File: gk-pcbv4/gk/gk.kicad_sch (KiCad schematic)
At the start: 11 parts

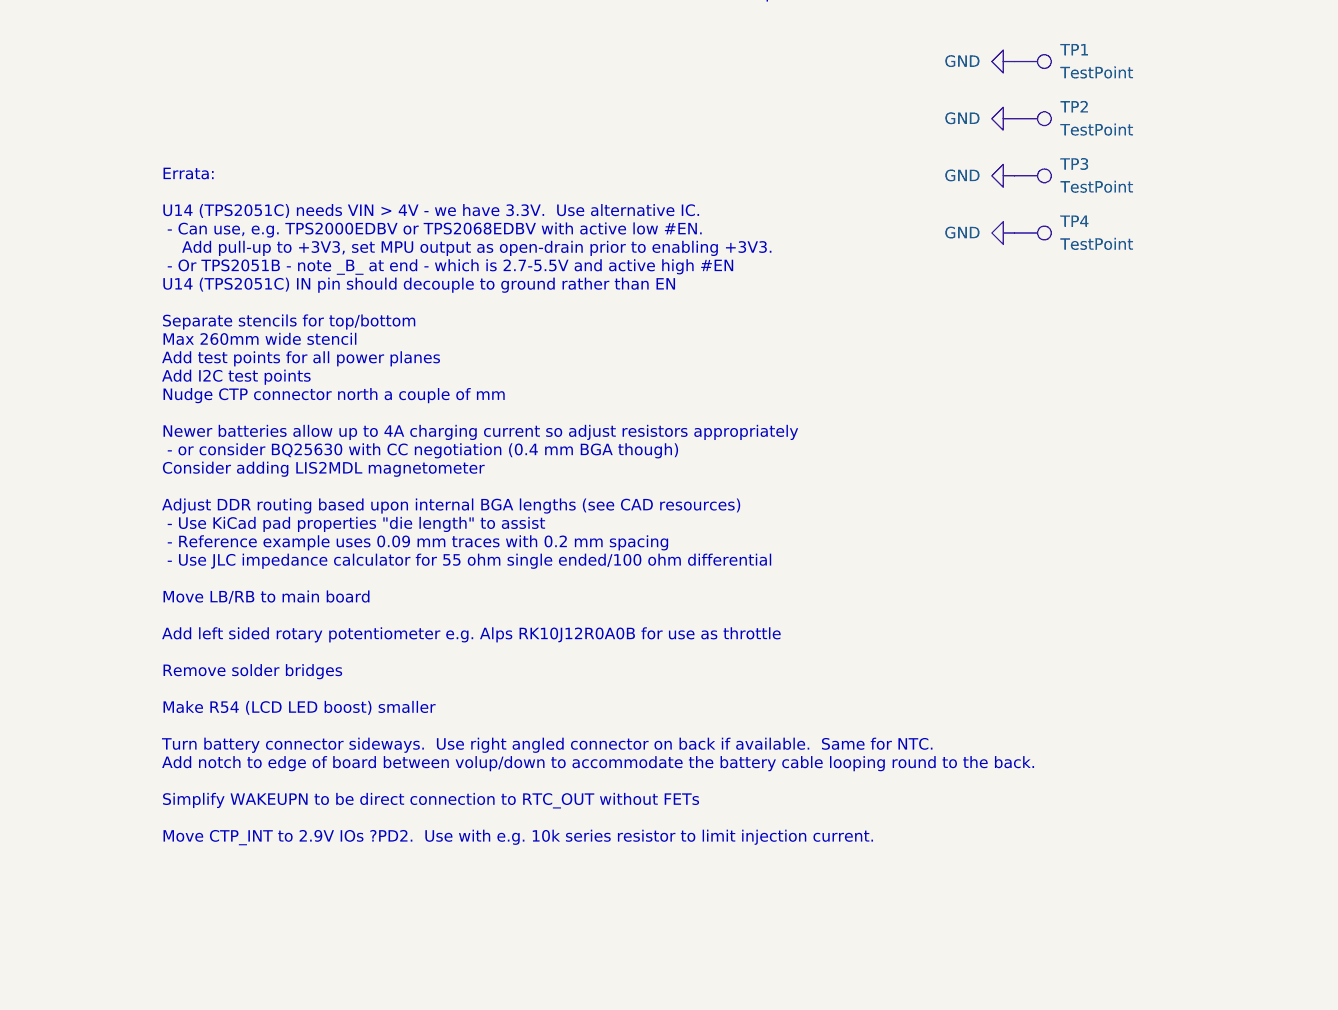
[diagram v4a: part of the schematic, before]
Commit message: Remove wakeupn mosfets in schematic
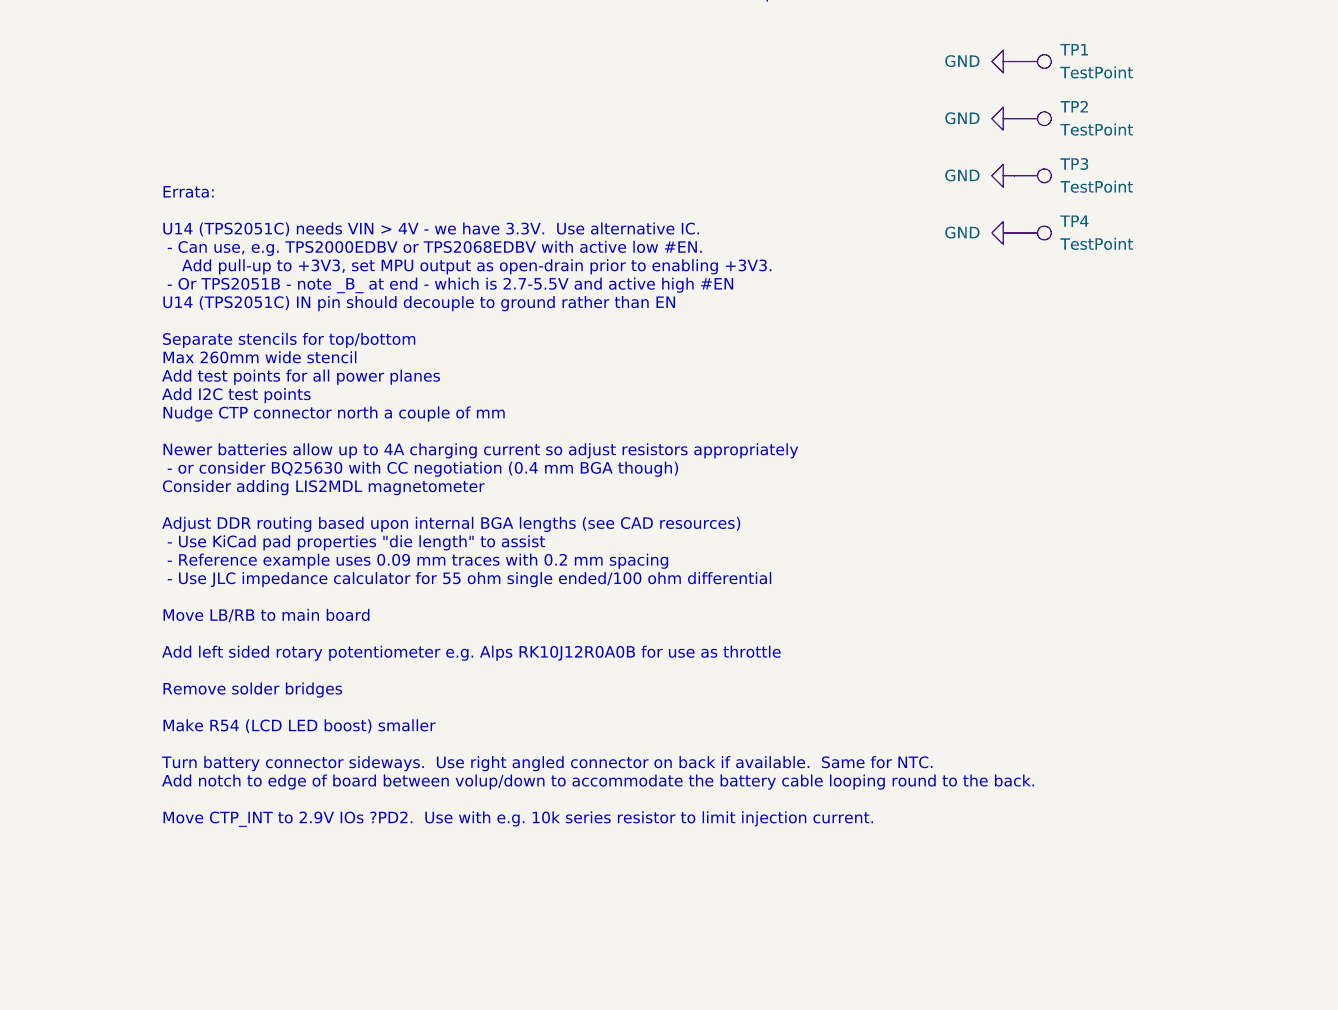
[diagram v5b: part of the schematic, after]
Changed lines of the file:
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@@
 		)
 	)
-	(text "Errata:\n\nU14 (TPS2051C) needs VIN > 4V - we have 3.3V.  Use alternative IC.\n - Can use, e.g. TPS2000EDBV or TPS2068EDBV with active low #EN.\n    Add pull-up to +3V3, set MPU output as open-drain prior to enabling +3V3.\n - Or TPS2051B - note _B_ at end - which is 2.7-5.5V and active high #EN\nU14 (TPS2051C) IN pin should decouple to ground rather than EN\n\nSeparate stencils for top/bottom\nMax 260mm wide stencil\nAdd test points for all power planes\nAdd I2C test points\nNudge CTP connector north a couple of mm\n\nNewer batteries allow up to 4A charging current so adjust resistors appropriately\n - or consider BQ25630 with CC negotiation (0.4 mm BGA though)\nConsider adding LIS2MDL magnetometer\n\nAdjust DDR routing based upon internal BGA lengths (see CAD resources)\n - Use KiCad pad properties \"die length\" to assist\n - Reference example uses 0.09 mm traces with 0.2 mm spacing\n - Use JLC impedance calculator for 55 ohm single ended/100 ohm differential\n\nMove LB/RB to main board\n\nAdd left sided rotary potentiometer e.g. Alps RK10J12R0A0B for use as throttle\n\nRemove solder bridges\n\nMake R54 (LCD LED boost) smaller\n\nTurn battery connector sideways.  Use right angled connector on back if available.  Same for NTC.\nAdd notch to edge of board between volup/down to accommodate the battery cable looping round to the back.\n\nSimplify WAKEUPN to be direct connection to RTC_OUT without FETs\n\nMove CTP_INT to 2.9V IOs ?PD2.  Use with e.g. 10k series resistor to limit injection current."
+	(text "Errata:\n\nU14 (TPS2051C) needs VIN > 4V - we have 3.3V.  Use alternative IC.\n - Can use, e.g. TPS2000EDBV or TPS2068EDBV with active low #EN.\n    Add pull-up to +3V3, set MPU output as open-drain prior to enabling +3V3.\n - Or TPS2051B - note _B_ at end - which is 2.7-5.5V and active high #EN\nU14 (TPS2051C) IN pin should decouple to ground rather than EN\n\nSeparate stencils for top/bottom\nMax 260mm wide stencil\nAdd test points for all power planes\nAdd I2C test points\nNudge CTP connector north a couple of mm\n\nNewer batteries allow up to 4A charging current so adjust resistors appropriately\n - or consider BQ25630 with CC negotiation (0.4 mm BGA though)\nConsider adding LIS2MDL magnetometer\n\nAdjust DDR routing based upon internal BGA lengths (see CAD resources)\n - Use KiCad pad properties \"die length\" to assist\n - Reference example uses 0.09 mm traces with 0.2 mm spacing\n - Use JLC impedance calculator for 55 ohm single ended/100 ohm differential\n\nMove LB/RB to main board\n\nAdd left sided rotary potentiometer e.g. Alps RK10J12R0A0B for use as throttle\n\nRemove solder bridges\n\nMake R54 (LCD LED boost) smaller\n\nTurn battery connector sideways.  Use right angled connector on back if available.  Same for NTC.\nAdd notch to edge of board between volup/down to accommodate the battery cable looping round to the back.\n\nMove CTP_INT to 2.9V IOs ?PD2.  Use with e.g. 10k series resistor to limit injection current."
 		(exclude_from_sim no)
 		(at 104.648 80.01 0)

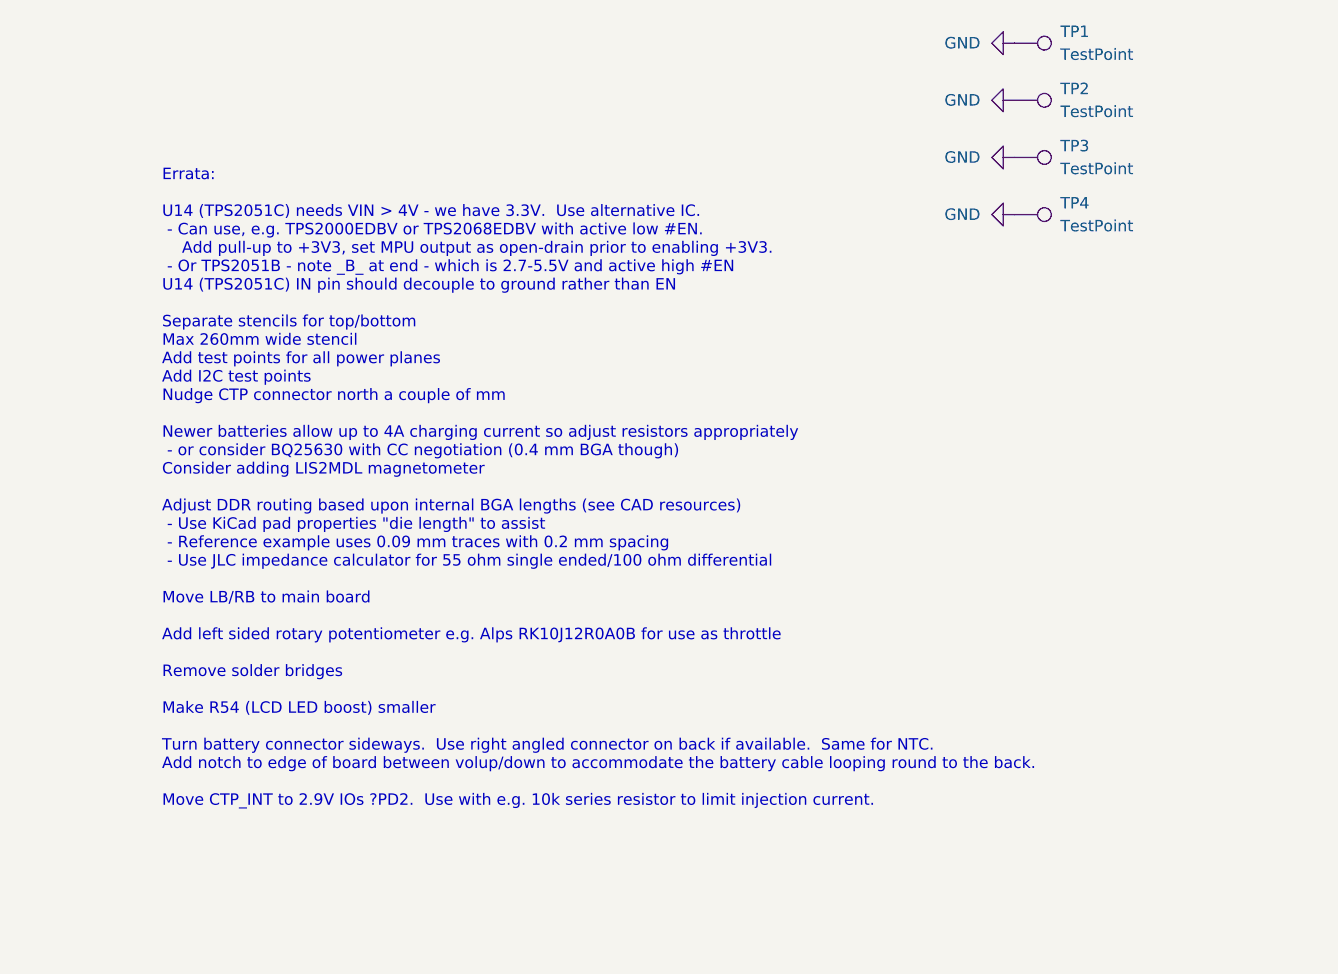
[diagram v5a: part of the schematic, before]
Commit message: update ctp irq resistor divider
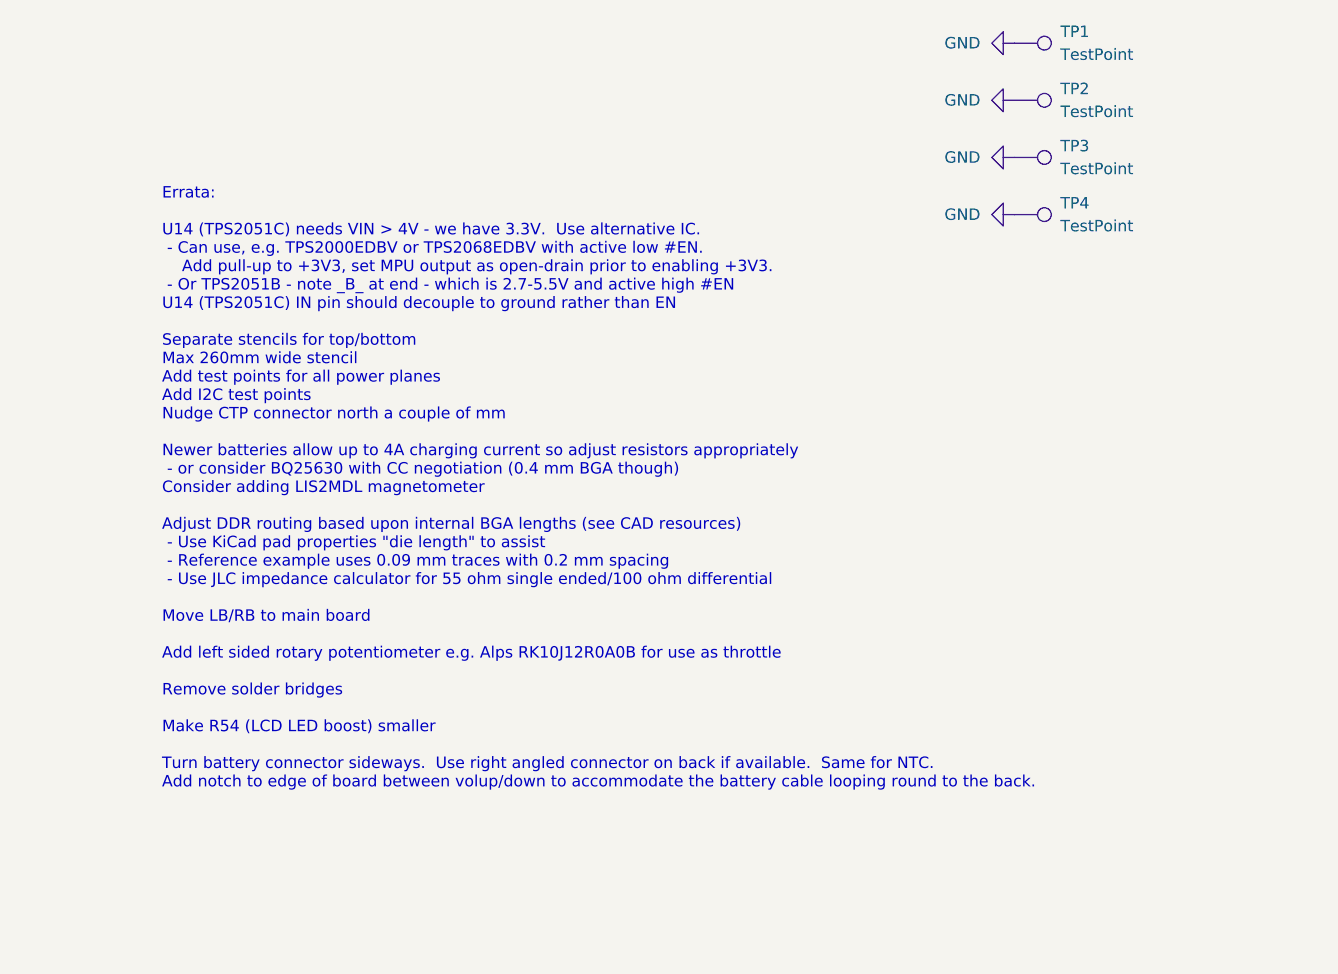
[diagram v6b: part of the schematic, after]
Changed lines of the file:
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@@
 		)
 	)
-	(text "Errata:\n\nU14 (TPS2051C) needs VIN > 4V - we have 3.3V.  Use alternative IC.\n - Can use, e.g. TPS2000EDBV or TPS2068EDBV with active low #EN.\n    Add pull-up to +3V3, set MPU output as open-drain prior to enabling +3V3.\n - Or TPS2051B - note _B_ at end - which is 2.7-5.5V and active high #EN\nU14 (TPS2051C) IN pin should decouple to ground rather than EN\n\nSeparate stencils for top/bottom\nMax 260mm wide stencil\nAdd test points for all power planes\nAdd I2C test points\nNudge CTP connector north a couple of mm\n\nNewer batteries allow up to 4A charging current so adjust resistors appropriately\n - or consider BQ25630 with CC negotiation (0.4 mm BGA though)\nConsider adding LIS2MDL magnetometer\n\nAdjust DDR routing based upon internal BGA lengths (see CAD resources)\n - Use KiCad pad properties \"die length\" to assist\n - Reference example uses 0.09 mm traces with 0.2 mm spacing\n - Use JLC impedance calculator for 55 ohm single ended/100 ohm differential\n\nMove LB/RB to main board\n\nAdd left sided rotary potentiometer e.g. Alps RK10J12R0A0B for use as throttle\n\nRemove solder bridges\n\nMake R54 (LCD LED boost) smaller\n\nTurn battery connector sideways.  Use right angled connector on back if available.  Same for NTC.\nAdd notch to edge of board between volup/down to accommodate the battery cable looping round to the back.\n\nMove CTP_INT to 2.9V IOs ?PD2.  Use with e.g. 10k series resistor to limit injection current."
+	(text "Errata:\n\nU14 (TPS2051C) needs VIN > 4V - we have 3.3V.  Use alternative IC.\n - Can use, e.g. TPS2000EDBV or TPS2068EDBV with active low #EN.\n    Add pull-up to +3V3, set MPU output as open-drain prior to enabling +3V3.\n - Or TPS2051B - note _B_ at end - which is 2.7-5.5V and active high #EN\nU14 (TPS2051C) IN pin should decouple to ground rather than EN\n\nSeparate stencils for top/bottom\nMax 260mm wide stencil\nAdd test points for all power planes\nAdd I2C test points\nNudge CTP connector north a couple of mm\n\nNewer batteries allow up to 4A charging current so adjust resistors appropriately\n - or consider BQ25630 with CC negotiation (0.4 mm BGA though)\nConsider adding LIS2MDL magnetometer\n\nAdjust DDR routing based upon internal BGA lengths (see CAD resources)\n - Use KiCad pad properties \"die length\" to assist\n - Reference example uses 0.09 mm traces with 0.2 mm spacing\n - Use JLC impedance calculator for 55 ohm single ended/100 ohm differential\n\nMove LB/RB to main board\n\nAdd left sided rotary potentiometer e.g. Alps RK10J12R0A0B for use as throttle\n\nRemove solder bridges\n\nMake R54 (LCD LED boost) smaller\n\nTurn battery connector sideways.  Use right angled connector on back if available.  Same for NTC.\nAdd notch to edge of board between volup/down to accommodate the battery cable looping round to the back.\n"
 		(exclude_from_sim no)
 		(at 104.648 80.01 0)
